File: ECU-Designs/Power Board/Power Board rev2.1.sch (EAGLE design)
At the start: 55 parts, among them X1 MINIFIT_5566-2, X2 MINIFIT_5566-6

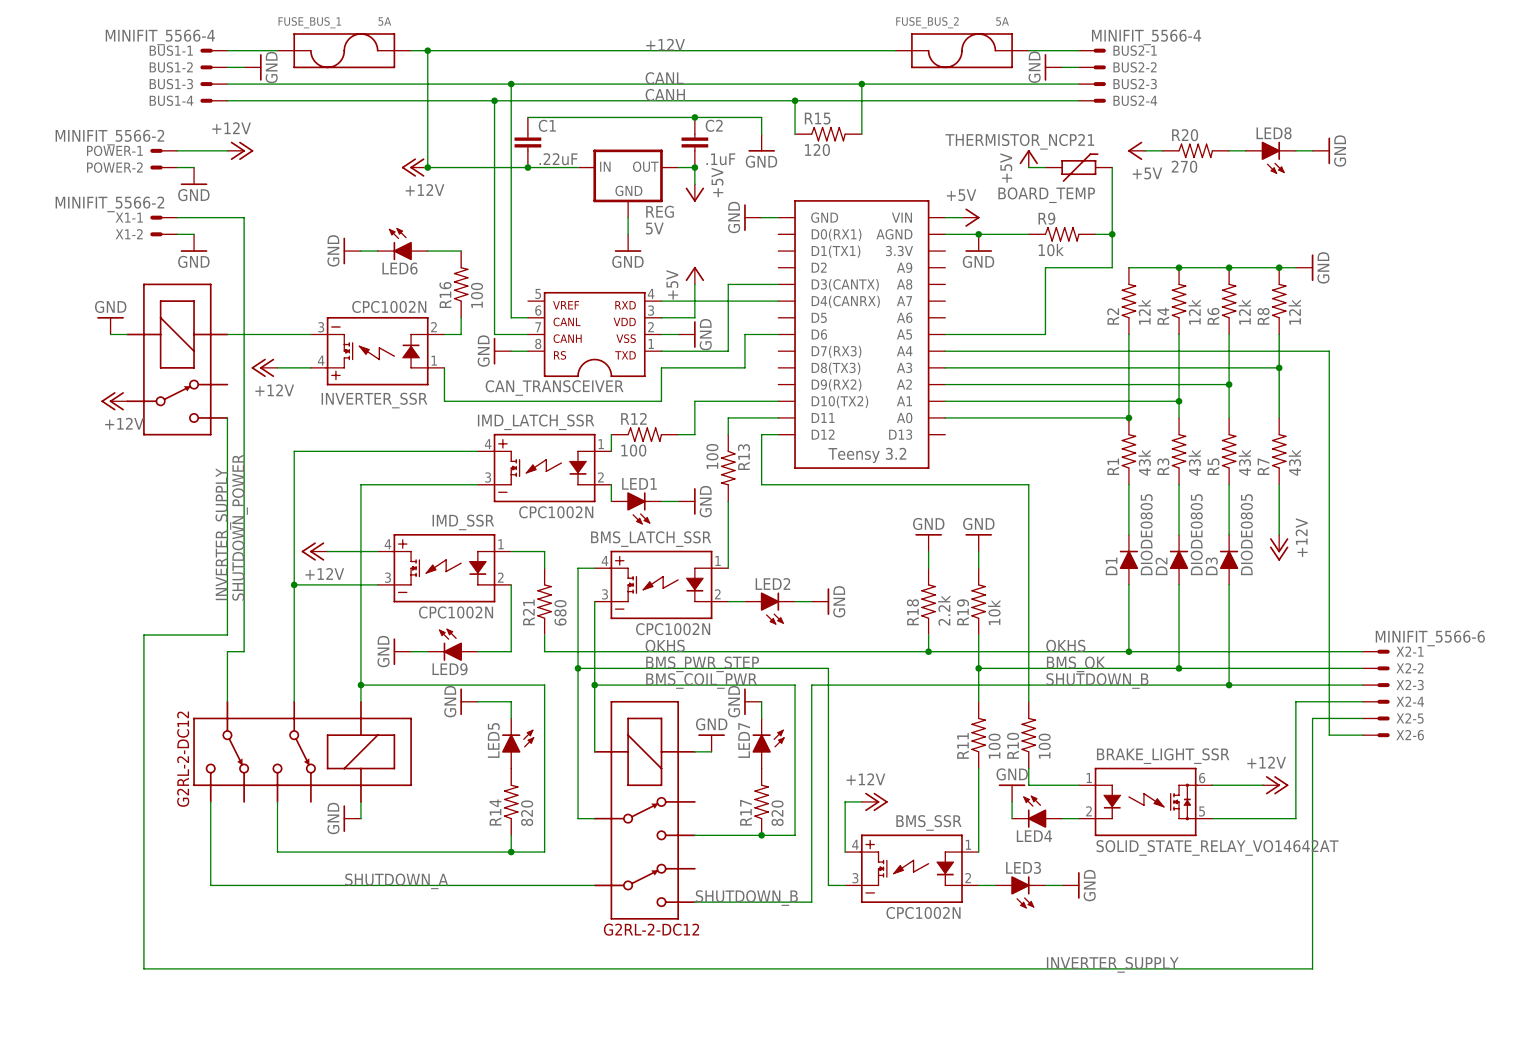
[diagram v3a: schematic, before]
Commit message: Add flyback diodes to relays
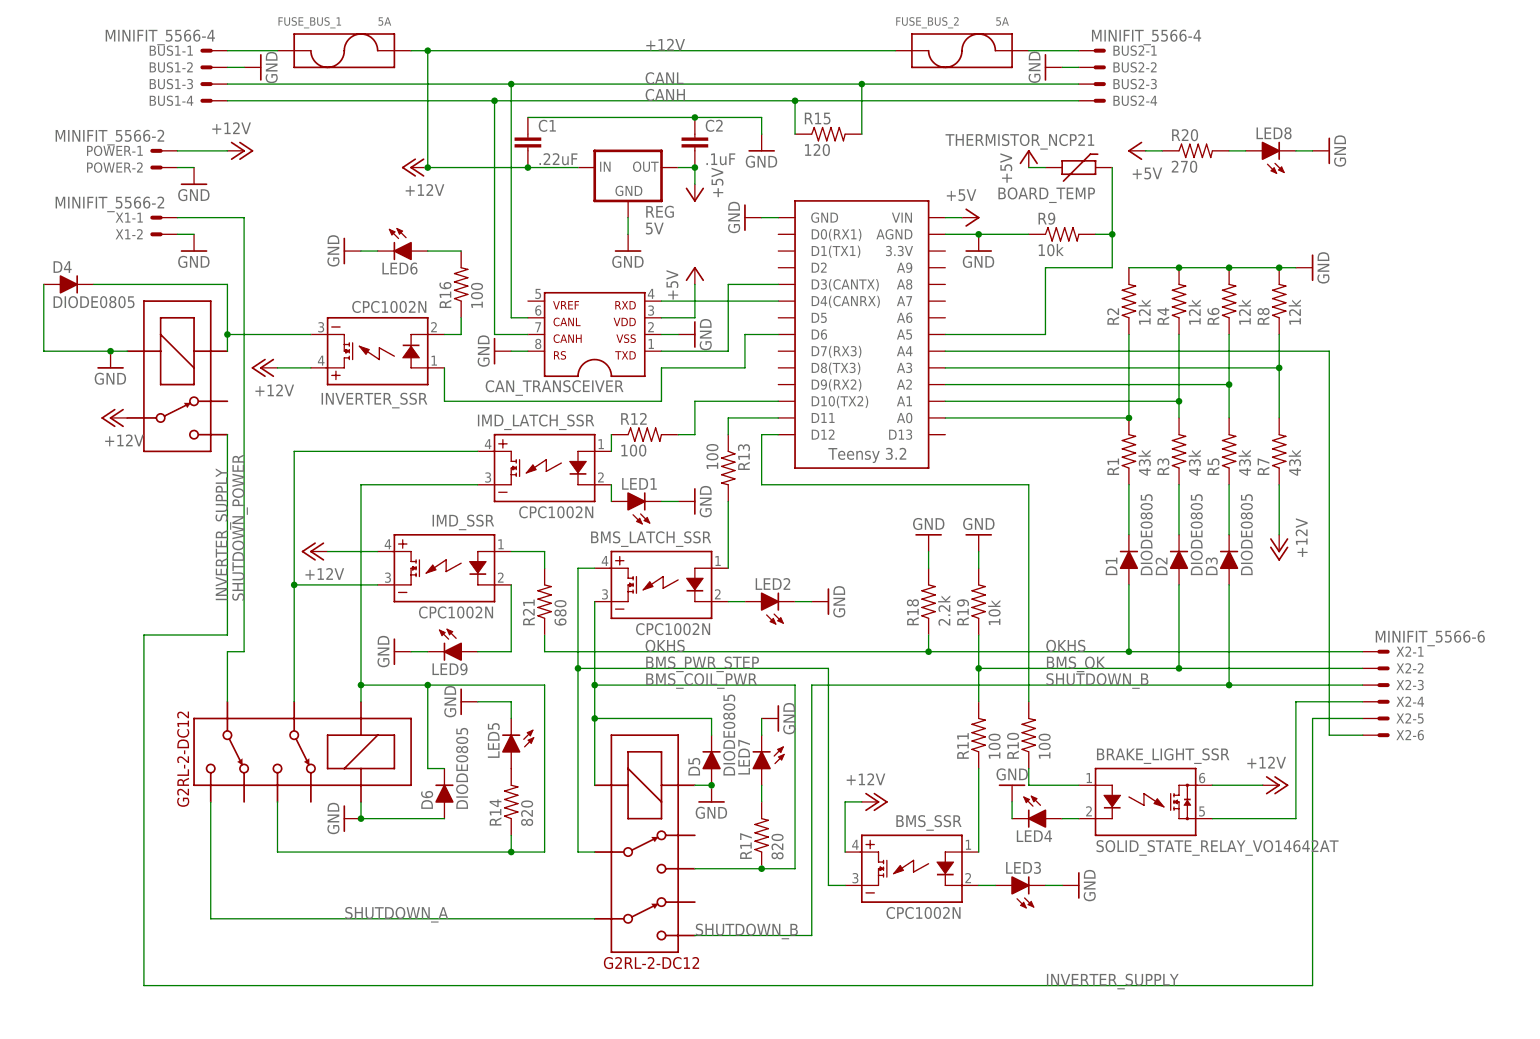
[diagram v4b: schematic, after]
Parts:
- added D4, D5, D6: DIODE0805, HyTechDevices:DIODE0805
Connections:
- net BMS_COIL_PWR: now also D5.C
- net GND: now also D4.A, D5.A, D6.A
- net N$26: now also D4.C
- net N$6: now also D6.C
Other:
- moved on the sheet: LED7, R17
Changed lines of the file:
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@@
 <part name="X1" library="HyTechDevices" deviceset="MINIFIT_5566-2" device=""/>
 <part name="GND25" library="HyTechSymbols" deviceset="GND" device=""/>
+<part name="D4" library="HyTechDevices" deviceset="DIODE" device="0805"/>
+<part name="D5" library="HyTechDevices" deviceset="DIODE" device="0805"/>
+<part name="D6" library="HyTechDevices" deviceset="DIODE" device="0805"/>
 </parts>
 <sheets>
@@
 <instance part="C2" gate="G$1" x="73.66" y="111.76"/>
 <instance part="GND7" gate="1" x="83.82" y="111.76"/>
-<instance part="U$1" gate="G$1" x="-7.62" y="88.9" rot="R270"/>
-<instance part="GND8" gate="1" x="-15.24" y="86.36" rot="R180"/>
+<instance part="U$1" gate="G$1" x="-7.62" y="86.36" rot="R270"/>
+<instance part="GND8" gate="1" x="-15.24" y="78.74"/>
 <instance part="X2" gate="-1" x="177.8" y="35.56"/>
 <instance part="X2" gate="-2" x="177.8" y="33.02"/>
@@
 <instance part="GND9" gate="1" x="20.32" y="96.52" rot="R270"/>
 <instance part="R16" gate="G$1" x="38.1" y="91.44" rot="R90"/>
-<instance part="IMD_SHUTDOWN1" gate="G$1" x="63.5" y="25.4" rot="R270"/>
-<instance part="GND19" gate="1" x="76.2" y="22.86" rot="R180"/>
-<instance part="R17" gate="G$1" x="83.82" y="12.7" rot="R90"/>
-<instance part="LED7" gate="LED" x="83.82" y="20.32" rot="R180"/>
-<instance part="GND20" gate="1" x="81.28" y="27.94" rot="R270"/>
+<instance part="IMD_SHUTDOWN1" gate="G$1" x="63.5" y="20.32" rot="R270"/>
+<instance part="GND19" gate="1" x="76.2" y="12.7"/>
+<instance part="R17" gate="G$1" x="83.82" y="7.62" rot="R90"/>
+<instance part="LED7" gate="LED" x="83.82" y="17.78" rot="R180"/>
+<instance part="GND20" gate="1" x="86.36" y="25.4" rot="R90"/>
 <instance part="P+1" gate="1" x="73.66" y="93.98"/>
 <instance part="P+2" gate="1" x="124.46" y="111.76"/>
@@
 <instance part="R21" gate="G$1" x="50.8" y="43.18" rot="R90"/>
 <instance part="P+7" gate="1" x="5.08" y="111.76" rot="R270"/>
-<instance part="P+8" gate="1" x="-15.24" y="73.66" rot="R90"/>
+<instance part="P+8" gate="1" x="-15.24" y="71.12" rot="R90"/>
 <instance part="P+9" gate="1" x="7.62" y="78.74" rot="R90"/>
 <instance part="P+10" gate="1" x="15.24" y="50.8" rot="R90"/>
@@
 <instance part="X1" gate="-1" x="-7.62" y="101.6" rot="MR0"/>
 <instance part="GND25" gate="1" x="-2.54" y="96.52"/>
+<instance part="D4" gate="1" x="-20.32" y="91.44"/>
+<instance part="D5" gate="1" x="76.2" y="20.32" rot="R90"/>
+<instance part="D6" gate="1" x="35.56" y="15.24" rot="R90"/>
 </instances>
 <busses>
@@
 <pinref part="GND13" gate="1" pin="GND"/>
 <wire x1="22.86" y1="10.16" x2="22.86" y2="12.7" width="0.1524" layer="91"/>
+<pinref part="D6" gate="1" pin="A"/>
+<wire x1="22.86" y1="10.16" x2="35.56" y2="10.16" width="0.1524" layer="91"/>
+<junction x="22.86" y="10.16"/>
 </segment>
 <segment>
@@
 <pinref part="U$1" gate="G$1" pin="COIL-"/>
 <pinref part="GND8" gate="1" pin="GND"/>
-<wire x1="-15.24" y1="83.82" x2="-12.7" y2="83.82" width="0.1524" layer="91"/>
+<wire x1="-15.24" y1="81.28" x2="-12.7" y2="81.28" width="0.1524" layer="91"/>
+<pinref part="D4" gate="1" pin="A"/>
+<wire x1="-25.4" y1="91.44" x2="-25.4" y2="81.28" width="0.1524" layer="91"/>
+<wire x1="-25.4" y1="81.28" x2="-15.24" y2="81.28" width="0.1524" layer="91"/>
+<junction x="-15.24" y="81.28"/>
 </segment>
 <segment>
@@
 </segment>
 <segment>
+<pinref part="GND19" gate="1" pin="GND"/>
+<pinref part="D5" gate="1" pin="A"/>
 <pinref part="IMD_SHUTDOWN1" gate="G$1" pin="COIL+"/>
-<pinref part="GND19" gate="1" pin="GND"/>
-<wire x1="73.66" y1="20.32" x2="76.2" y2="20.32" width="0.1524" layer="91"/>
+<wire x1="76.2" y1="15.24" x2="73.66" y2="15.24" width="0.1524" layer="91"/>
+<junction x="76.2" y="15.24"/>
 </segment>
 <segment>
 <pinref part="GND20" gate="1" pin="GND"/>
 <pinref part="LED7" gate="LED" pin="C"/>
-<wire x1="83.82" y1="27.94" x2="83.82" y2="25.4" width="0.1524" layer="91"/>
+<wire x1="83.82" y1="25.4" x2="83.82" y2="22.86" width="0.1524" layer="91"/>
 </segment>
 <segment>
@@
 <pinref part="IMD_LATCH_SSR" gate="G$1" pin="DC-"/>
 <wire x1="22.86" y1="60.96" x2="40.64" y2="60.96" width="0.1524" layer="91"/>
-<wire x1="50.8" y1="30.48" x2="22.86" y2="30.48" width="0.1524" layer="91"/>
+<wire x1="50.8" y1="30.48" x2="33.02" y2="30.48" width="0.1524" layer="91"/>
 <pinref part="R14" gate="G$1" pin="1"/>
+<wire x1="33.02" y1="30.48" x2="22.86" y2="30.48" width="0.1524" layer="91"/>
 <wire x1="45.72" y1="7.62" x2="45.72" y2="5.08" width="0.1524" layer="91"/>
 <junction x="45.72" y="5.08"/>
+<wire x1="33.02" y1="30.48" x2="33.02" y2="17.78" width="0.1524" layer="91"/>
+<pinref part="D6" gate="1" pin="C"/>
+<wire x1="33.02" y1="17.78" x2="35.56" y2="17.78" width="0.1524" layer="91"/>
+<junction x="33.02" y="30.48"/>
 </segment>
 </net>
@@
 <junction x="154.94" y="30.48"/>
 <pinref part="IMD_SHUTDOWN1" gate="G$1" pin="5"/>
-<wire x1="73.66" y1="-2.54" x2="91.44" y2="-2.54" width="0.1524" layer="91"/>
-<wire x1="91.44" y1="-2.54" x2="91.44" y2="30.48" width="0.1524" layer="91"/>
-<label x="73.66" y="-2.54" size="1.778" layer="95"/>
+<wire x1="73.66" y1="-7.62" x2="91.44" y2="-7.62" width="0.1524" layer="91"/>
+<wire x1="91.44" y1="-7.62" x2="91.44" y2="30.48" width="0.1524" layer="91"/>
+<label x="73.66" y="-7.62" size="1.778" layer="95"/>
 </segment>
 </net>
@@
 <segment>
 <pinref part="U$1" gate="G$1" pin="S"/>
-<wire x1="2.54" y1="71.12" x2="2.54" y2="38.1" width="0.1524" layer="91"/>
+<wire x1="2.54" y1="68.58" x2="2.54" y2="38.1" width="0.1524" layer="91"/>
 <wire x1="2.54" y1="38.1" x2="-10.16" y2="38.1" width="0.1524" layer="91"/>
-<wire x1="-10.16" y1="38.1" x2="-10.16" y2="-12.7" width="0.1524" layer="91"/>
-<wire x1="-10.16" y1="-12.7" x2="167.64" y2="-12.7" width="0.1524" layer="91"/>
-<wire x1="167.64" y1="-12.7" x2="167.64" y2="25.4" width="0.1524" layer="91"/>
+<wire x1="-10.16" y1="38.1" x2="-10.16" y2="-15.24" width="0.1524" layer="91"/>
+<wire x1="-10.16" y1="-15.24" x2="167.64" y2="-15.24" width="0.1524" layer="91"/>
+<wire x1="167.64" y1="-15.24" x2="167.64" y2="25.4" width="0.1524" layer="91"/>
 <pinref part="X2" gate="-5" pin="S"/>
 <wire x1="167.64" y1="25.4" x2="175.26" y2="25.4" width="0.1524" layer="91"/>
-<label x="127" y="-12.7" size="1.778" layer="95"/>
+<label x="127" y="-15.24" size="1.778" layer="95"/>
 <label x="2.54" y="43.18" size="1.778" layer="95" rot="R90"/>
 </segment>
@@
 <pinref part="INVERTER_SSR" gate="G$1" pin="DC-"/>
 <pinref part="U$1" gate="G$1" pin="COIL+"/>
+<pinref part="D4" gate="1" pin="C"/>
+<wire x1="-17.78" y1="91.44" x2="2.54" y2="91.44" width="0.1524" layer="91"/>
+<wire x1="2.54" y1="91.44" x2="2.54" y2="83.82" width="0.1524" layer="91"/>
+<wire x1="2.54" y1="83.82" x2="2.54" y2="81.28" width="0.1524" layer="91"/>
 <wire x1="15.24" y1="83.82" x2="2.54" y2="83.82" width="0.1524" layer="91"/>
+<junction x="2.54" y="83.82"/>
 </segment>
 </net>
@@
 <segment>
 <pinref part="IMD_SHUTDOWN1" gate="G$1" pin="COIL-"/>
-<wire x1="58.42" y1="20.32" x2="58.42" y2="30.48" width="0.1524" layer="91"/>
+<wire x1="58.42" y1="15.24" x2="58.42" y2="25.4" width="0.1524" layer="91"/>
 <pinref part="BMS_LATCH_SSR" gate="G$1" pin="DC-"/>
 <pinref part="IMD_SHUTDOWN1" gate="G$1" pin="4"/>
+<wire x1="58.42" y1="25.4" x2="58.42" y2="30.48" width="0.1524" layer="91"/>
 <wire x1="58.42" y1="30.48" x2="58.42" y2="43.18" width="0.1524" layer="91"/>
-<wire x1="73.66" y1="7.62" x2="83.82" y2="7.62" width="0.1524" layer="91"/>
-<wire x1="83.82" y1="7.62" x2="88.9" y2="7.62" width="0.1524" layer="91"/>
-<wire x1="88.9" y1="7.62" x2="88.9" y2="30.48" width="0.1524" layer="91"/>
-<wire x1="88.9" y1="30.48" x2="58.42" y2="30.48" width="0.1524" layer="91"/>
+<wire x1="73.66" y1="2.54" x2="83.82" y2="2.54" width="0.1524" layer="91"/>
+<wire x1="83.82" y1="2.54" x2="88.9" y2="2.54" width="0.1524" layer="91"/>
+<wire x1="88.9" y1="2.54" x2="88.9" y2="30.48" width="0.1524" layer="91"/>
 <junction x="58.42" y="30.48"/>
 <pinref part="R17" gate="G$1" pin="1"/>
-<junction x="83.82" y="7.62"/>
+<junction x="83.82" y="2.54"/>
 <label x="66.04" y="30.48" size="1.778" layer="95"/>
+<wire x1="88.9" y1="30.48" x2="58.42" y2="30.48" width="0.1524" layer="91"/>
+<pinref part="D5" gate="1" pin="C"/>
+<wire x1="76.2" y1="22.86" x2="76.2" y2="25.4" width="0.1524" layer="91"/>
+<wire x1="76.2" y1="25.4" x2="58.42" y2="25.4" width="0.1524" layer="91"/>
+<junction x="58.42" y="25.4"/>
 </segment>
 </net>
@@
 <wire x1="55.88" y1="48.26" x2="55.88" y2="33.02" width="0.1524" layer="91"/>
 <pinref part="IMD_SHUTDOWN1" gate="G$1" pin="3"/>
-<wire x1="55.88" y1="33.02" x2="55.88" y2="10.16" width="0.1524" layer="91"/>
-<wire x1="55.88" y1="10.16" x2="58.42" y2="10.16" width="0.1524" layer="91"/>
+<wire x1="55.88" y1="33.02" x2="55.88" y2="5.08" width="0.1524" layer="91"/>
+<wire x1="55.88" y1="5.08" x2="58.42" y2="5.08" width="0.1524" layer="91"/>
 <pinref part="BMS_SSR" gate="G$1" pin="DC-"/>
 <wire x1="96.52" y1="0" x2="93.98" y2="0" width="0.1524" layer="91"/>
@@
 <pinref part="IMD_SHUTDOWN1" gate="G$1" pin="6"/>
 <pinref part="IMD_SHUTDOWN" gate="G$1" pin="5"/>
-<wire x1="0" y1="12.7" x2="0" y2="0" width="0.1524" layer="91"/>
-<wire x1="0" y1="0" x2="58.42" y2="0" width="0.1524" layer="91"/>
-<label x="20.32" y="0" size="1.778" layer="95"/>
+<wire x1="0" y1="12.7" x2="0" y2="-5.08" width="0.1524" layer="91"/>
+<wire x1="0" y1="-5.08" x2="58.42" y2="-5.08" width="0.1524" layer="91"/>
+<label x="20.32" y="-5.08" size="1.778" layer="95"/>
 </segment>
 </net>
@@
 <pinref part="R17" gate="G$1" pin="2"/>
 <pinref part="LED7" gate="LED" pin="A"/>
-</segment>
-</net>
+<wire x1="83.82" y1="12.7" x2="83.82" y2="15.24" width="0.1524" layer="91"/>
+</segment>
+</net>
